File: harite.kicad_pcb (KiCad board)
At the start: 2 copper layers, 126.5 x 92.8 mm, 33 parts, among them J1 Cirque Connector, U1 RP2040_Zero

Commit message: cleanup
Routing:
- net GND: track 0.00 -> 2.95 mm
- net Row 2: track 174.1 -> 176.5 mm, vias 6 -> 8
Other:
- board size 126.5 x 92.8 mm -> 125.9 x 92 mm

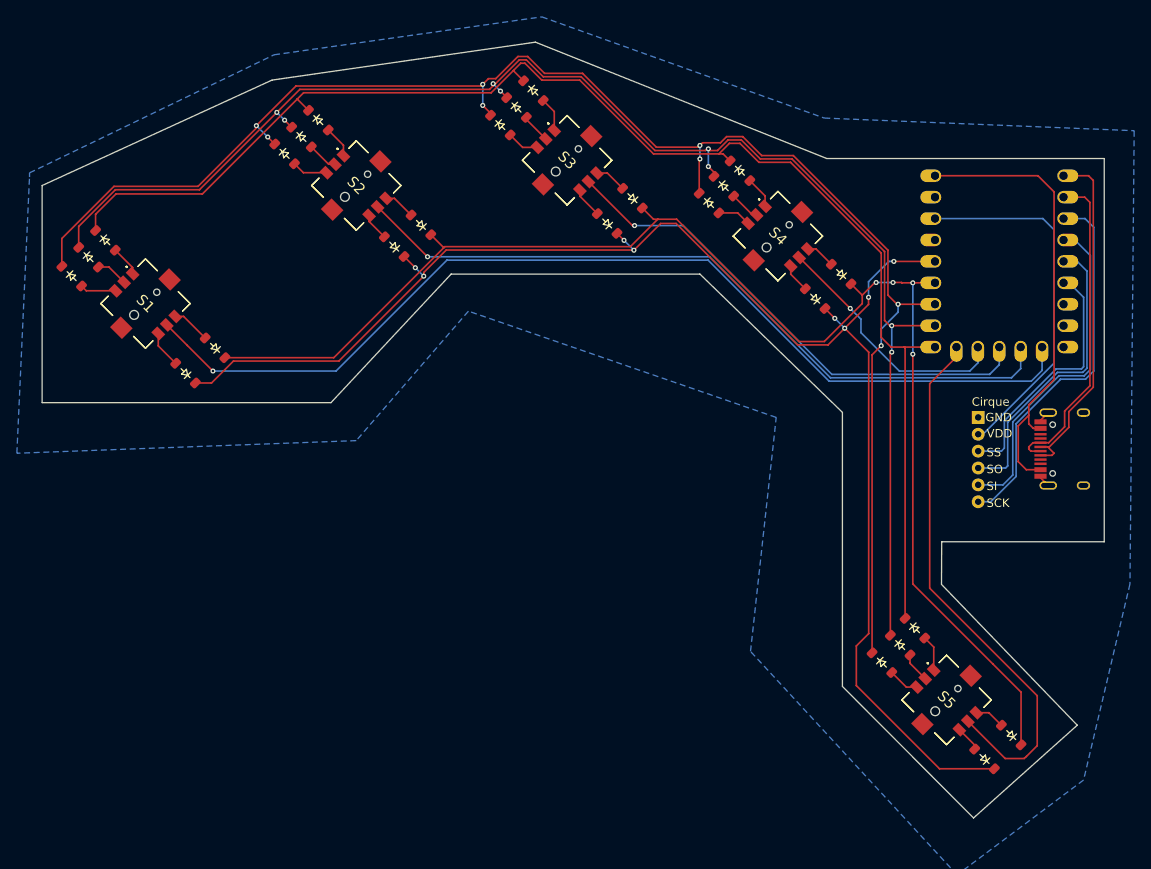
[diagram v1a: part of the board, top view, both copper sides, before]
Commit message: mounting holes
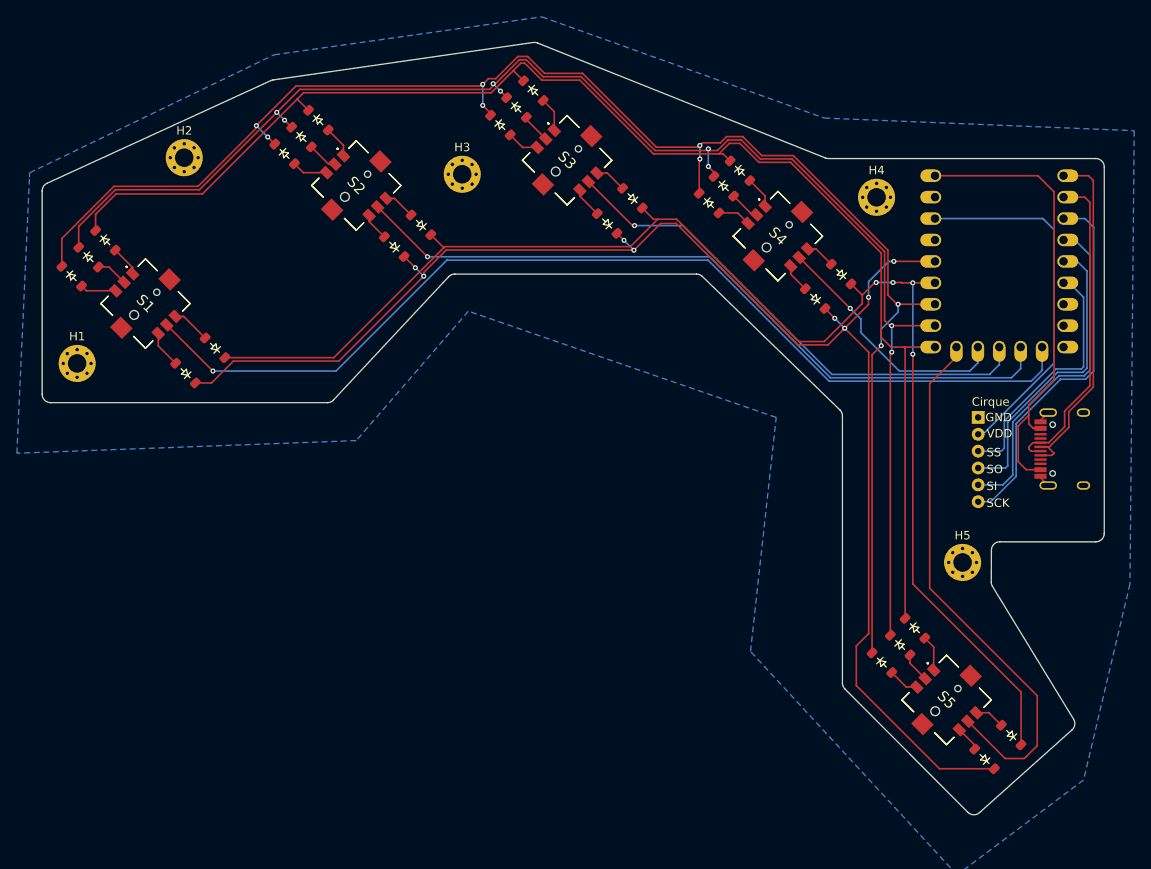
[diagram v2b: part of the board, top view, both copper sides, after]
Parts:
- added H1: Mounting_Hole, MountingHole:MountingHole_2.2mm_M2_Pad_Via, F.Cu at (91.9, 107.1)
- added H2: Mounting_Hole, MountingHole:MountingHole_2.2mm_M2_Pad_Via, F.Cu at (104.6, 82.7)
- added H3: Mounting_Hole, MountingHole:MountingHole_2.2mm_M2_Pad_Via, F.Cu at (137.6, 84.7)
- added H4: Mounting_Hole, MountingHole:MountingHole_2.2mm_M2_Pad_Via, F.Cu at (186.7, 87.4)
- added H5: Mounting_Hole, MountingHole:MountingHole_2.2mm_M2_Pad_Via, F.Cu at (196.9, 130.7)
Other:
- board size 125.9 x 92 mm -> 125.9 x 91.6 mm

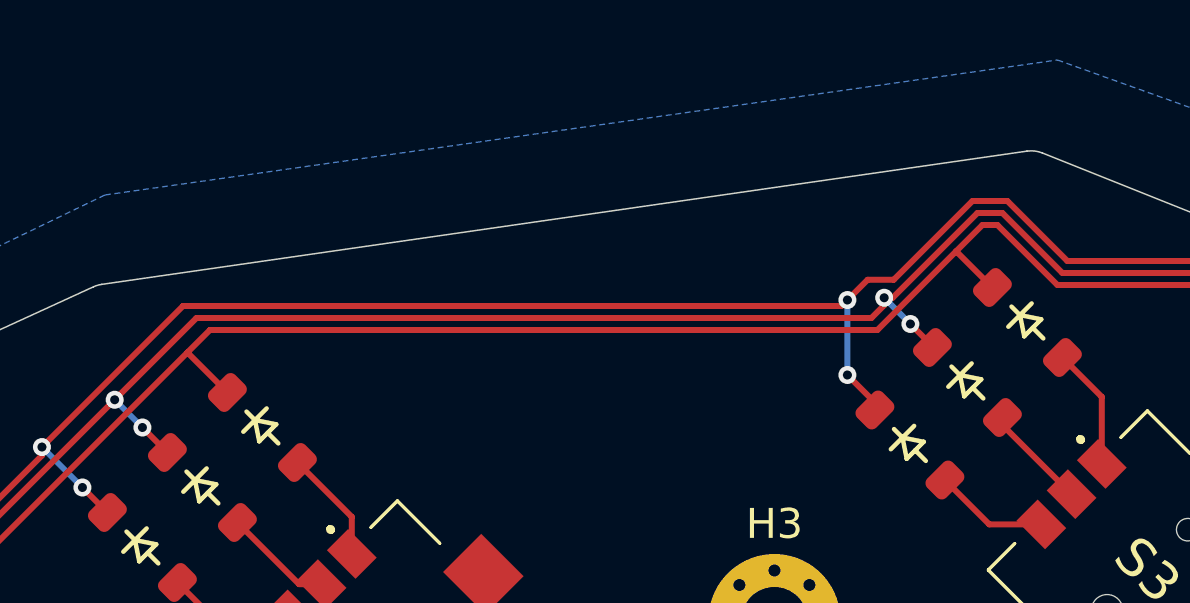
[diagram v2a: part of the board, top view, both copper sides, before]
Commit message: Use skrhade switch model
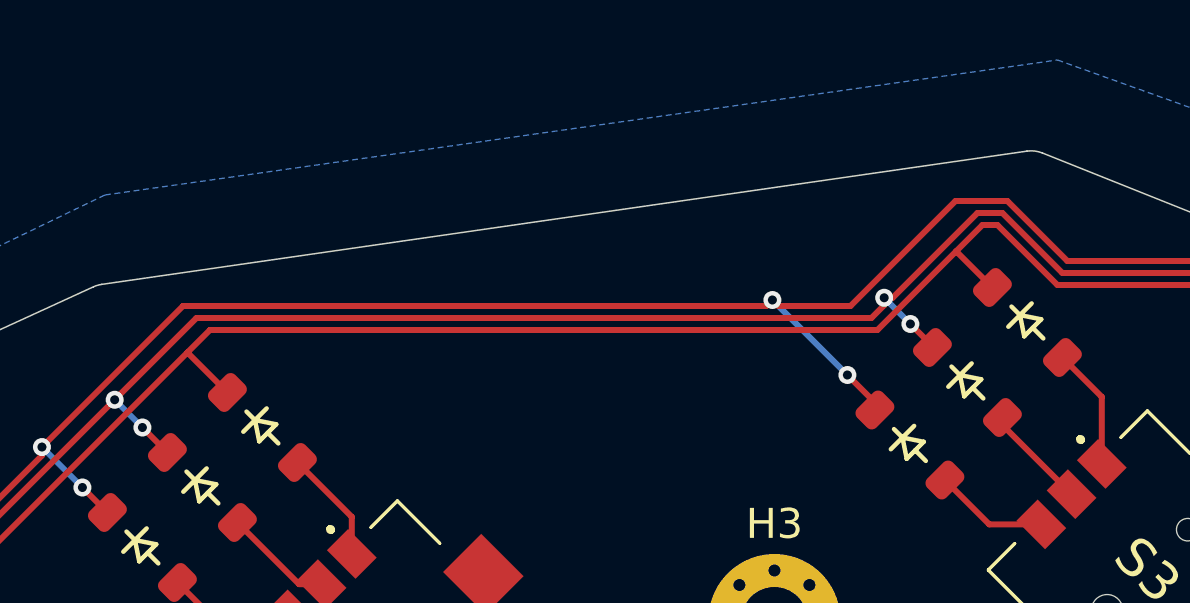
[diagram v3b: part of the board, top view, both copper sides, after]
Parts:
- S1, S2, S3, S4, S5: footprint footprints:SKRHADE010 -> footprints:SKRHADE
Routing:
- net Row 3: track 187.7 -> 188.9 mm
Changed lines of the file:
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@@
 		)
 	)
-	(footprint "footprints:SKRHADE010"
+	(footprint "footprints:SKRHADE"
 		(layer "F.Cu")
 		(at 150 83 -45)
@@
 		(tags "Switch")
 		(property "Reference" "S3"
-			(at 0 0 135)
+			(at 0 0 -45)
 			(layer "F.SilkS")
 			(effects
@@
 		)
 		(property "Value" "SKRHADE010"
-			(at 0 0 135)
+			(at 0 0 -45)
 			(layer "F.SilkS")
 			(hide yes)
@@
 			)
 		)
-		(property "Footprint" "footprints:SKRHADE010"
+		(property "Footprint" "footprints:SKRHADE"
 			(at 0 0 -45)
 			(unlocked yes)
@@
 		)
 		(fp_text user "${REFERENCE}"
-			(at 0 0 135)
+			(at 0 0 -45)
 			(layer "F.Fab")
 			(effects
@@
 			(pintype "passive")
 		)
-		(model "SKRHADE010.stp"
+		(model "SKRHADE.step"
 			(offset
 				(xyz 0 0 0)
@@
 		)
 	)
-	(footprint "footprints:SKRHADE010"
+	(footprint "footprints:SKRHADE"
 		(layer "F.Cu")
 		(at 175 92 -45)
@@
 		(tags "Switch")
 		(property "Reference" "S4"
-			(at 0 0 135)
+			(at 0 0 -45)
 			(layer "F.SilkS")
 			(effects
@@
 		)
 		(property "Value" "SKRHADE010"
-			(at 0 0 135)
+			(at 0 0 -45)
 			(layer "F.SilkS")
 			(hide yes)
@@
 			)
 		)
-		(property "Footprint" "footprints:SKRHADE010"
+		(property "Footprint" "footprints:SKRHADE"
 			(at 0 0 -45)
 			(unlocked yes)
@@
 		)
 		(fp_text user "${REFERENCE}"
-			(at 0 0 135)
+			(at 0 0 -45)
 			(layer "F.Fab")
 			(effects
@@
 			(pintype "passive")
 		)
-		(model "SKRHADE010.stp"
+		(model "SKRHADE.step"
 			(offset
 				(xyz 0 0 0)
@@
 		)
 	)
-	(footprint "footprints:SKRHADE010"
+	(footprint "footprints:SKRHADE"
 		(layer "F.Cu")
 		(at 125 86 -45)
@@
 		(tags "Switch")
 		(property "Reference" "S2"
-			(at 0 0 135)
+			(at 0 0 -45)
 			(layer "F.SilkS")
 			(effects
@@
 		)
 		(property "Value" "SKRHADE010"
-			(at 0 0 135)
+			(at 0 0 -45)
 			(layer "F.SilkS")
 			(hide yes)
@@
 			)
 		)
-		(property "Footprint" "footprints:SKRHADE010"
+		(property "Footprint" "footprints:SKRHADE"
 			(at 0 0 -45)
 			(unlocked yes)
@@
 		)
 		(fp_text user "${REFERENCE}"
-			(at 0 0 135)
+			(at 0 0 -45)
 			(layer "F.Fab")
 			(effects
@@
 			(pintype "passive")
 		)
-		(model "SKRHADE010.stp"
+		(model "SKRHADE.step"
 			(offset
 				(xyz 0 0 0)
@@
 		)
 	)
-	(footprint "footprints:SKRHADE010"
+	(footprint "footprints:SKRHADE"
 		(layer "F.Cu")
 		(at 100 100 -45)
@@
 		(tags "Switch")
 		(property "Reference" "S1"
-			(at 0 0 135)
+			(at 0 0 -45)
 			(layer "F.SilkS")
 			(effects
@@
 		)
 		(property "Value" "SKRHADE010"
-			(at 0 0 135)
+			(at 0 0 -45)
 			(layer "F.SilkS")
 			(hide yes)
@@
 			)
 		)
-		(property "Footprint" "footprints:SKRHADE010"
+		(property "Footprint" "footprints:SKRHADE"
 			(at 0 0 -45)
 			(unlocked yes)
@@
 		)
 		(fp_text user "${REFERENCE}"
-			(at 0 0 135)
+			(at 0 0 -45)
 			(layer "F.Fab")
 			(effects
@@
 			(pintype "passive")
 		)
-		(model "SKRHADE010.stp"
+		(model "SKRHADE.step"
 			(offset
 				(xyz 0 0 0)
@@
 		)
 	)
-	(footprint "footprints:SKRHADE010"
+	(footprint "footprints:SKRHADE"
 		(layer "F.Cu")
 		(at 195 147 -45)
@@
 		(tags "Switch")
 		(property "Reference" "S5"
-			(at 0 0 135)
+			(at 0 0 -45)
 			(layer "F.SilkS")
 			(effects
@@
 		)
 		(property "Value" "SKRHADE010"
-			(at 0 0 135)
+			(at 0 0 -45)
 			(layer "F.SilkS")
 			(hide yes)
@@
 			)
 		)
-		(property "Footprint" "footprints:SKRHADE010"
+		(property "Footprint" "footprints:SKRHADE"
 			(at 0 0 -45)
 			(unlocked yes)
@@
 		)
 		(fp_text user "${REFERENCE}"
-			(at 0 0 135)
+			(at 0 0 -45)
 			(layer "F.Fab")
 			(effects
@@
 			(pintype "passive")
 		)
-		(model "SKRHADE010.stp"
+		(model "SKRHADE.step"
 			(offset
 				(xyz 0 0 0)
@@
 	)
 	(segment
+		(start 137.5 74)
+		(end 137.7 74.2)
+		(width 0.2)
+		(layer "F.Cu")
+		(net 9)
+	)
+	(segment
 		(start 165.666548 86.916548)
 		(end 165.666548 82.933452)
@@
 	)
 	(segment
-		(start 144.168631 70.7)
-		(end 145.331372 70.7)
+		(start 145.331372 70.7)
+		(end 147.331372 72.7)
 		(width 0.2)
 		(layer "F.Cu")
@@
 	)
 	(segment
-		(start 113.15147 79.184314)
-		(end 113.15147 78.90147)
+		(start 165.55 81.45)
+		(end 165.75 81.25)
 		(width 0.2)
 		(layer "F.Cu")
@@
 	)
 	(segment
-		(start 147.331372 72.7)
-		(end 151.831372 72.7)
+		(start 113.15147 79.184314)
+		(end 113.15147 78.90147)
 		(width 0.2)
 		(layer "F.Cu")
@@
 	)
 	(segment
+		(start 160.581372 81.45)
+		(end 165.55 81.45)
+		(width 0.2)
+		(layer "F.Cu")
+		(net 9)
+	)
+	(segment
 		(start 186.166548 106.083452)
 		(end 187.25 105)
@@
 	)
 	(segment
-		(start 139.8 74.2)
+		(start 137.3 74.2)
 		(end 117.852941 74.2)
 		(width 0.2)
@@
 	)
 	(segment
+		(start 137.7 74.2)
+		(end 140.10294 74.2)
+		(width 0.2)
+		(layer "F.Cu")
+		(net 9)
+	)
+	(segment
 		(start 188.05 99)
 		(end 189.13 100.08)
@@
 	)
 	(segment
-		(start 140.674265 73.325735)
-		(end 141.542896 73.325735)
+		(start 151.831372 72.7)
+		(end 160.581372 81.45)
 		(width 0.2)
 		(layer "F.Cu")
@@
 	)
 	(segment
-		(start 160.581372 81.45)
-		(end 165.55 81.45)
+		(start 117.852941 74.2)
+		(end 113.15147 78.90147)
 		(width 0.2)
 		(layer "F.Cu")
@@
 	)
 	(segment
-		(start 140 74)
-		(end 140.674265 73.325735)
-		(width 0.2)
-		(layer "F.Cu")
-		(net 9)
-	)
-	(segment
 		(start 170.831372 80.2)
 		(end 173.081372 82.45)
@@
 	)
 	(segment
-		(start 173.081372 82.45)
-		(end 176.831372 82.45)
+		(start 137.5 74)
+		(end 137.3 74.2)
 		(width 0.2)
 		(layer "F.Cu")
@@
 	)
 	(segment
-		(start 140 74)
-		(end 139.8 74.2)
-		(width 0.2)
-		(layer "F.Cu")
-		(net 9)
-	)
-	(segment
-		(start 141.542896 73.325735)
-		(end 144.168631 70.7)
+		(start 173.081372 82.45)
+		(end 176.831372 82.45)
 		(width 0.2)
 		(layer "F.Cu")
@@
 	)
 	(segment
-		(start 117.852941 74.2)
-		(end 113.15147 78.90147)
-		(width 0.2)
-		(layer "F.Cu")
-		(net 9)
-	)
-	(segment
-		(start 151.831372 72.7)
-		(end 160.581372 81.45)
+		(start 147.331372 72.7)
+		(end 151.831372 72.7)
 		(width 0.2)
 		(layer "F.Cu")
@@
 	)
 	(segment
-		(start 165.55 81.45)
-		(end 165.75 81.25)
+		(start 140.10294 74.2)
+		(end 143.60294 70.7)
 		(width 0.2)
 		(layer "F.Cu")
@@
 	)
 	(segment
-		(start 145.331372 70.7)
-		(end 147.331372 72.7)
+		(start 90.083274 95.583274)
+		(end 90.083274 92.285355)
 		(width 0.2)
 		(layer "F.Cu")
@@
 	)
 	(segment
-		(start 90.083274 95.583274)
-		(end 90.083274 92.285355)
+		(start 143.60294 70.7)
+		(end 145.331372 70.7)
 		(width 0.2)
 		(layer "F.Cu")
@@
 	)
 	(via
-		(at 140 74)
+		(at 137.5 74)
 		(size 0.6)
 		(drill 0.3)
@@
 	)
 	(segment
-		(start 140 74)
-		(end 140 76.5)
+		(start 187.25 103.021471)
+		(end 189.25 101.021471)
 		(width 0.2)
 		(layer "B.Cu")
@@
 	)
 	(segment
-		(start 187.25 103.021471)
-		(end 189.25 101.021471)
+		(start 137.5 74)
+		(end 140 76.5)
 		(width 0.2)
 		(layer "B.Cu")

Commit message: Mirror sides
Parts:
- added D26: D, ScottoKeebs_Components:Diode_SOD-123, F.Cu at (361.9, -1.40)
- added D27: D, ScottoKeebs_Components:Diode_SOD-123, F.Cu at (361.9, 1.95)
- added D28: D, ScottoKeebs_Components:Diode_SOD-123, F.Cu at (361.9, 5.30)
- added D29: D, ScottoKeebs_Components:Diode_SOD-123, F.Cu at (361.9, 8.65)
- added D30: D, ScottoKeebs_Components:Diode_SOD-123, F.Cu at (361.9, 12.0)
- added D31: D, ScottoKeebs_Components:Diode_SOD-123, F.Cu at (361.9, 15.3)
- added D32: D, ScottoKeebs_Components:Diode_SOD-123, F.Cu at (361.9, 18.7)
- added D33: D, ScottoKeebs_Components:Diode_SOD-123, F.Cu at (367.7, -1.40)
- added D34: D, ScottoKeebs_Components:Diode_SOD-123, F.Cu at (367.7, 1.95)
- added D35: D, ScottoKeebs_Components:Diode_SOD-123, F.Cu at (367.7, 5.30)
- added D36: D, ScottoKeebs_Components:Diode_SOD-123, F.Cu at (367.7, 8.65)
- added D37: D, ScottoKeebs_Components:Diode_SOD-123, F.Cu at (367.7, 12.0)
- added D38: D, ScottoKeebs_Components:Diode_SOD-123, F.Cu at (367.7, 15.3)
- added D39: D, ScottoKeebs_Components:Diode_SOD-123, F.Cu at (367.7, 18.7)
- added D40: D, ScottoKeebs_Components:Diode_SOD-123, F.Cu at (373.4, -1.40)
- added D41: D, ScottoKeebs_Components:Diode_SOD-123, F.Cu at (373.4, 1.95)
- added D42: D, ScottoKeebs_Components:Diode_SOD-123, F.Cu at (373.4, 5.30)
- added D43: D, ScottoKeebs_Components:Diode_SOD-123, F.Cu at (373.4, 8.65)
- added D44: D, ScottoKeebs_Components:Diode_SOD-123, F.Cu at (373.4, 12.0)
- added D45: D, ScottoKeebs_Components:Diode_SOD-123, F.Cu at (373.4, 15.3)
- added D46: D, ScottoKeebs_Components:Diode_SOD-123, F.Cu at (373.4, 18.7)
- added D47: D, ScottoKeebs_Components:Diode_SOD-123, F.Cu at (379.2, -1.40)
- added D48: D, ScottoKeebs_Components:Diode_SOD-123, F.Cu at (379.2, 1.95)
- added D49: D, ScottoKeebs_Components:Diode_SOD-123, F.Cu at (379.2, 5.30)
- added D50: D, ScottoKeebs_Components:Diode_SOD-123, F.Cu at (379.2, 8.65)
- added H10: Mounting_Hole, MountingHole:MountingHole_2.2mm_M2_Pad_Via, F.Cu at (236.8, 130.7)
- added H6: Mounting_Hole, MountingHole:MountingHole_2.2mm_M2_Pad_Via, F.Cu at (341.8, 107.1)
- added H7: Mounting_Hole, MountingHole:MountingHole_2.2mm_M2_Pad_Via, F.Cu at (329.1, 82.7)
- added H8: Mounting_Hole, MountingHole:MountingHole_2.2mm_M2_Pad_Via, F.Cu at (296.1, 84.7)
- added H9: Mounting_Hole, MountingHole:MountingHole_2.2mm_M2_Pad_Via, F.Cu at (247.0, 87.4)
- added J2: Cirque Connector, footprints:Cirque-connector, F.Cu at (234.7, 119.2)
- added S10: SKRHADE010, footprints:SKRHADE, F.Cu at (238.7, 147.0)
- added S6: SKRHADE010, footprints:SKRHADE, F.Cu at (333.7, 100.0)
- added S7: SKRHADE010, footprints:SKRHADE, F.Cu at (308.7, 86.0)
- added S8: SKRHADE010, footprints:SKRHADE, F.Cu at (283.7, 83.0)
- added S9: SKRHADE010, footprints:SKRHADE, F.Cu at (258.7, 92.0)
- added U2: RP2040_Zero, ScottoKeebs_MCU:RP2040_Zero, F.Cu at (232.4, 95.0)
- added USB2: HRO-TYPE-C-31-M-12, footprints:HRO-TYPE-C-31-M-12, F.Cu at (219.9, 117.2)
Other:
- board size 125.9 x 91.6 mm -> 258.2 x 91.6 mm

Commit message: Organise diodes
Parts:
- moved D44 250.4 mm to (162.4, 146.9), turned to 45 degrees
- moved D45 248.0 mm to (164.5, 149.0), turned to 45 degrees
- moved D46 245.6 mm to (166.6, 151.0), turned to 45 degrees
- moved D49 242.5 mm to (174.7, 135.6), turned to -135 degrees
- moved D50 239.6 mm to (177.8, 138.5), turned to -135 degrees
- moved D41 211.2 mm to (182.4, 92.0), turned to 45 degrees
- moved D42 208.9 mm to (184.4, 94.2), turned to 45 degrees
- moved D43 206.5 mm to (186.5, 96.3), turned to 45 degrees
- moved D47 201.7 mm to (195.1, 80.9), turned to -135 degrees
- moved D48 198.9 mm to (197.8, 83.7), turned to -135 degrees
- moved D36 176.7 mm to (207.4, 83.1), turned to 45 degrees
- moved D37 174.3 mm to (209.4, 85.1), turned to 45 degrees
- moved D38 171.9 mm to (211.5, 87.1), turned to 45 degrees
- moved D40 168.5 mm to (223.2, 74.8), turned to -135 degrees
- moved D33 160.5 mm to (236.2, 90.6), turned to 45 degrees
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
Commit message: Connect diodes
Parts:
- moved D32 0.54 mm to (234.5, 88.2)
- moved D31 0.53 mm to (232.4, 86.1)
- moved D33 0.44 mm to (236.5, 90.3)
- moved D26 0.34 mm to (257.3, 100.2)
- moved D28 0.27 mm to (261.3, 104.1)
- moved D39 0.27 mm to (220.2, 72.0)
- moved D27 0.25 mm to (259.3, 102.2)
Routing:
- net RRow 3: track 0.00 -> 207.4 mm, vias 0 -> 6
- net RRow 5: track 0.00 -> 200.3 mm, vias 0 -> 10
- net RRow 2: track 0.00 -> 194.9 mm, vias 0 -> 8
- net RRow 1: track 0.00 -> 189.2 mm, vias 0 -> 2
- net RRow 4: track 0.00 -> 187.7 mm, vias 0 -> 4
- net RCol 1: track 0.00 -> 146.7 mm, vias 0 -> 1
- net RCol 2: track 0.00 -> 117.2 mm, vias 0 -> 1
- net RCol 3: track 0.00 -> 97.3 mm, vias 0 -> 1
- net RCol 5: track 0.00 -> 76.5 mm, vias 0 -> 3
- net RCol 4: track 0.00 -> 55.0 mm, vias 0 -> 1
- net Net-(D33-A): track 0.00 -> 4.02 mm
- net Net-(D43-A): track 0.00 -> 3.99 mm
- net Net-(D26-A): track 0.00 -> 3.99 mm
- net Net-(D28-A): track 0.00 -> 3.90 mm
- net Net-(D31-A): track 0.00 -> 3.89 mm
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
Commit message: Connect the rest
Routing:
- net RSCK: track 0.00 -> 57.9 mm, vias 0 -> 1
- net RGP0: track 0.00 -> 56.7 mm, vias 0 -> 1
- net RGP1: track 0.00 -> 55.5 mm, vias 0 -> 1
- net RSI: track 0.00 -> 53.3 mm, vias 0 -> 1
- net RSO: track 0.00 -> 50.4 mm
- net R5V: track 0.00 -> 47.6 mm, vias 0 -> 1
- net RSS: track 0.00 -> 45.6 mm
- net R3V3: track 0.00 -> 31.1 mm
- net RGND: track 0.00 -> 28.8 mm, vias 0 -> 2
- net RCol 2: track 117.2 -> 118.8 mm
- net RCol 3: track 97.3 -> 98.9 mm
- net RCol 5: track 76.5 -> 75.5 mm
- net RCol 1: track 146.7 -> 147.7 mm
- added copper zone on B.Cu, net RGND

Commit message: Fix ground
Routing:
- net RGND: track 28.8 -> 2.95 mm, vias 2 -> 0
- net 3V3: track 43.0 -> 40.2 mm, vias 0 -> 1
- net RGP0: track 56.7 -> 57.2 mm, vias 1 -> 2
- net RGP1: track 55.5 -> 56.0 mm, vias 1 -> 2
- net R5V: track 47.6 -> 47.8 mm, vias 1 -> 2
